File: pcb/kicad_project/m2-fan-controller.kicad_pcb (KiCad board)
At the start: 2 copper layers, 22 x 30 mm, 25 parts, among them J1 Bus_M.2_Socket_E, J2 JST PH_B4B-PH-K, J3 JST PH_B4B-PH-K, J4 JST PH_S2B-PH-K, J5 Conn_02x02_Odd_Even, U1 STM32F042F6P6, U2 TPS22810DBV, U3 TPS22810DBV

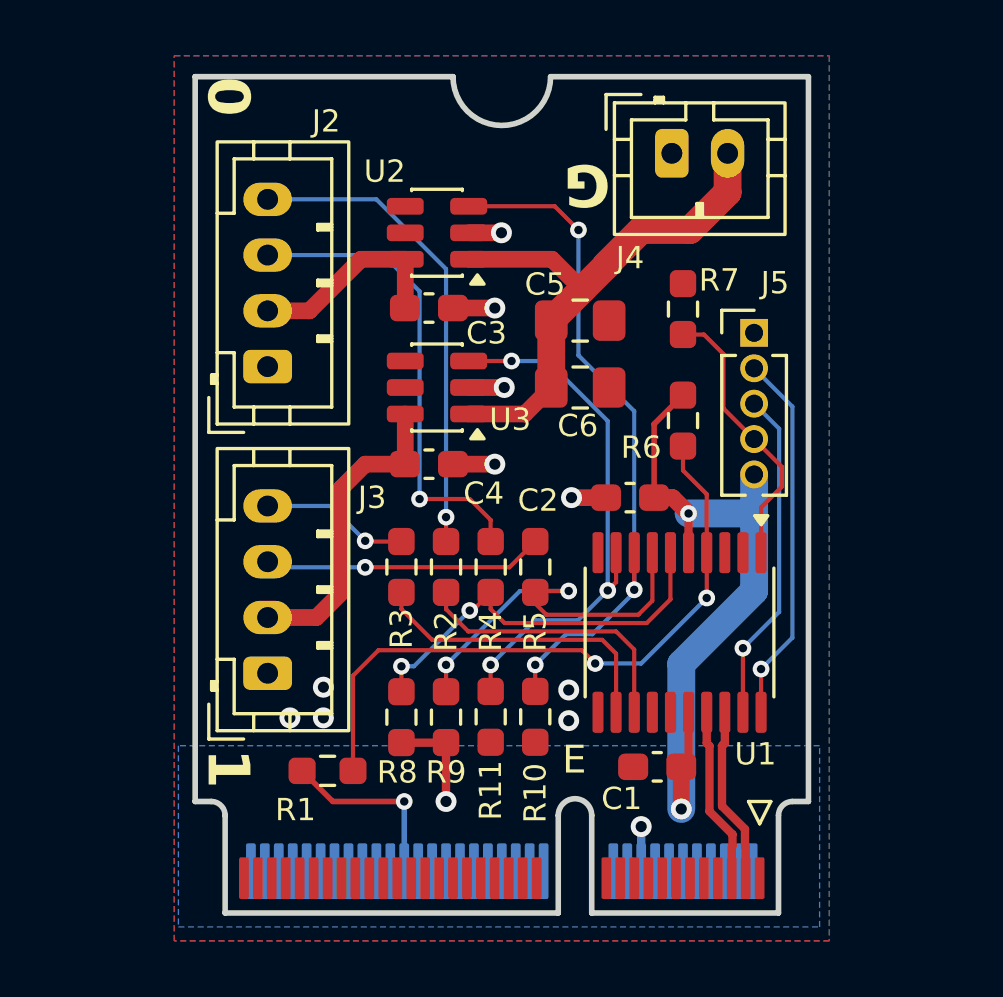
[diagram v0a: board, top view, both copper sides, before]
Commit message: Add 4-ouptut capability + low-frequency PWM control
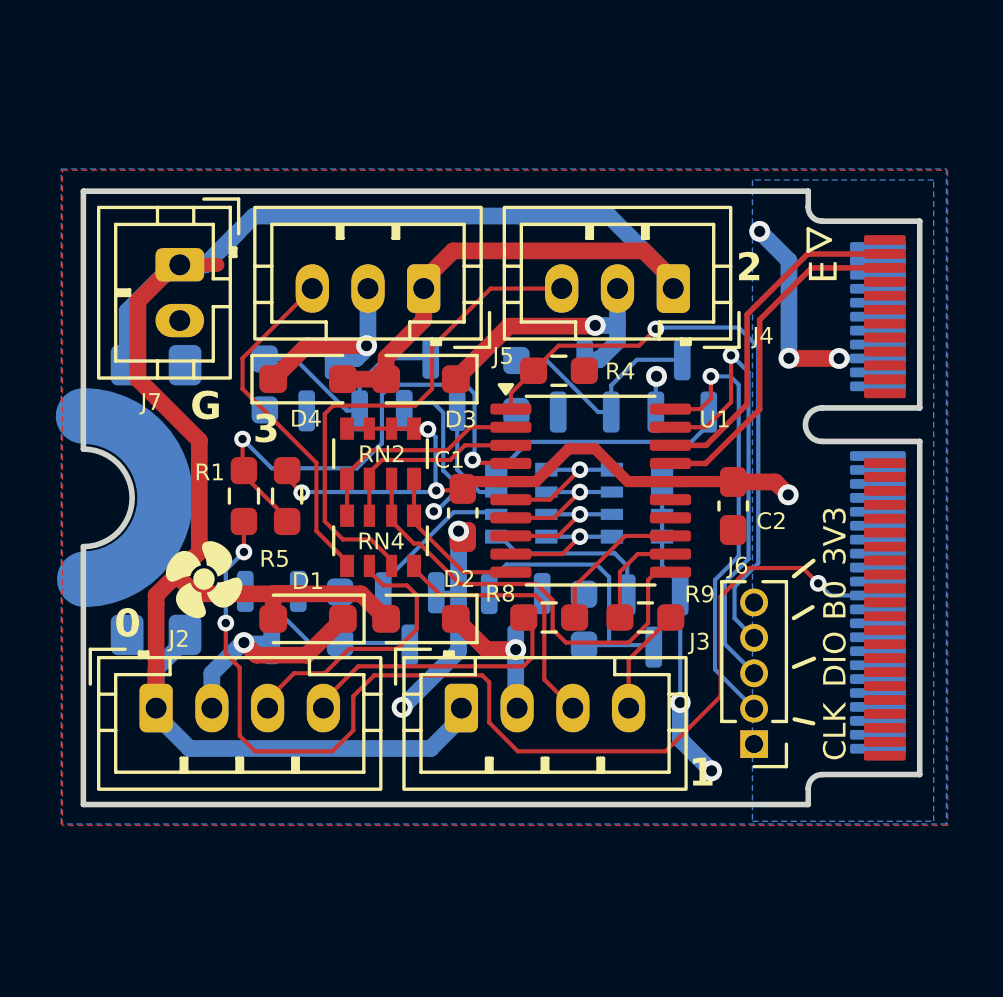
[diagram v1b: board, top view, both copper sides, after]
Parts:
- removed C5, C6: 1uF, Capacitor_SMD:C_0805_2012Metric_Pad1.18x1.45mm_HandSolder
- removed R10, R11: 10kOhm, Resistor_SMD:R_0603_1608Metric_Pad0.98x0.95mm_HandSolder
- removed U2, U3: TPS22810DBV, Package_TO_SOT_SMD:SOT-23-6
- added D1: GDB5819WS, Diode_SMD:D_SOD-323_HandSoldering, F.Cu at (132.1, 99.5)
- added D2: GDB5819WS, Diode_SMD:D_SOD-323_HandSoldering, F.Cu at (136.1, 99.5)
- added D3: GDB5819WS, Diode_SMD:D_SOD-323_HandSoldering, F.Cu at (136.1, 90.8)
- added D4: GDB5819WS, Diode_SMD:D_SOD-323_HandSoldering, F.Cu at (132.1, 90.8)
- added J4: JST PH_B3B-PH-K, Connector_JST:JST_PH_B3B-PH-K_1x03_P2.00mm_Vertical, F.Cu at (145.2, 87.6)
- added J5: JST PH_B3B-PH-K, Connector_JST:JST_PH_B3B-PH-K_1x03_P2.00mm_Vertical, F.Cu at (136.2, 87.6)
- added NT1: NetTie_2, NetTie:NetTie-2_SMD_Pad0.5mm, F.Cu at (128.3, 86.8)
- added Q1: BSS138, Package_TO_SOT_SMD:SOT-23, B.Cu at (135.7, 99.5)
- added Q2: AO3401A, Package_TO_SOT_SMD:SOT-23, B.Cu at (130.7, 99.4)
- added Q3: BSS138, Package_TO_SOT_SMD:SOT-23, B.Cu at (144.4, 99.5)
- added Q4: AO3401A, Package_TO_SOT_SMD:SOT-23, B.Cu at (139.5, 99.5)
- added Q5: BSS138, Package_TO_SOT_SMD:SOT-23, B.Cu at (145.5, 91.1)
- added Q6: AO3401A, Package_TO_SOT_SMD:SOT-23, B.Cu at (142.0, 91.1)
- added Q7: BSS138, Package_TO_SOT_SMD:SOT-23, B.Cu at (136.4, 91.0)
- added Q8: AO3401A, Package_TO_SOT_SMD:SOT-23, B.Cu at (132.9, 91.0)
- added RN1: 1kOhm, Resistor_SMD:R_Array_Convex_4x0603, B.Cu at (139.7, 95.3)
- added RN2: 10kOhm, Resistor_SMD:R_Array_Convex_4x0603, F.Cu at (134.7, 93.5)
- added RN3: 10kOhm, Resistor_SMD:R_Array_Convex_4x0603, B.Cu at (143.8, 95.3)
- added RN4: 100Ohm, Resistor_SMD:R_Array_Convex_4x0603, F.Cu at (134.7, 96.7)
- C3, C4: value 0.1uF -> 1uF; footprint Capacitor_SMD:C_0603_1608Metric_Pad1.08x0.95mm_HandSolder -> Capacitor_SMD:C_0805_2012Metric_Pad1.18x1.45mm_HandSolder; moved to B.Cu
- R2, R3: value 100Ohm -> 4.7kOhm; moved to B.Cu
- R4, R5: value 100Ohm -> 10kOhm
- R6, R7: value 10kOhm -> 4.7kOhm; moved to B.Cu
- R8: value 10kOhm -> 1kOhm
- R9: value 10kOhm -> 100Ohm
- moved J7 18.1 mm to (127.5, 86.8), turned to -90 degrees
- moved J1 15.5 mm to (150.0, 95.1), turned to 90 degrees
- moved R7 15.2 mm to (130.5, 91.0), turned to -90 degrees
- moved J6 14.8 mm to (148.1, 103.9), turned to 180 degrees
- moved J2 12.9 mm to (126.6, 102.7), turned to 0 degrees
- moved C4 11.5 mm to (126.6, 100.0)
- moved C1 11.5 mm to (137.6, 95.7), turned to -90 degrees
- moved R1 10.3 mm to (129.8, 95.0), turned to -90 degrees
- moved C3 10.00 mm to (126.6, 90.3), turned to 180 degrees
- moved R5 9.26 mm to (131.3, 95.0), turned to -90 degrees
- moved R9 7.99 mm to (144.2, 99.4), turned to 0 degrees
- moved R4 7.45 mm to (141.1, 90.5), turned to 0 degrees
- moved J3 7.06 mm to (137.6, 102.7), turned to 0 degrees
- moved R3 6.82 mm to (141.9, 99.5)
- moved R8 6.39 mm to (140.7, 99.4), turned to 180 degrees
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- renumbered J5 to J6, J4 to J7
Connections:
- net SWCLK renamed /SWCLK
- net SWDIO renamed /SWDIO
- net USB_D+ renamed /USB_D+
- net USB_D- renamed /USB_D-
- C1 pad 1: +3.3V -> 3V3
- C2 pad 1: +3.3V -> 3V3
- C3 pad 1: Net-(J2-Pin_2) -> 12V
- C3 pad 2: GND -> FGND
- C4 pad 1: Net-(J3-Pin_2) -> 12V
- C4 pad 2: GND -> FGND
- J1 pad 2: +3.3V -> 3V3
- J1 pad 4: +3.3V -> 3V3
- J1 pad 72: +3.3V -> 3V3
- J1 pad 74: +3.3V -> 3V3
- J2 pad 1: GND -> FGND
- J2 pad 2: Net-(J2-Pin_2) -> /POWER_0
- J3 pad 1: GND -> FGND
- J3 pad 2: Net-(J3-Pin_2) -> /POWER_1
- J6 pad 4: BOOT0 -> /BOOT0
- J6 pad 5: +3.3V -> 3V3
- J7 pad 1: GND -> FGND
- J7 pad 2: +12V -> 12V
- R1 pad 1: RST -> /RST
- R2 pad 1: PWM_0 -> Net-(Q1-D)
- R2 pad 2: Net-(J2-Pin_4) -> 12V
- R3 pad 1: PWM_1 -> Net-(Q3-D)
- R3 pad 2: Net-(J3-Pin_4) -> 12V
- R4 pad 1: TACH_0 -> /BOOT0
- R4 pad 2: Net-(J2-Pin_3) -> GND
- R5 pad 1: TACH_1 -> 3V3
- R5 pad 2: Net-(J3-Pin_3) -> /RST
- R6 pad 1: +3.3V -> Net-(Q5-D)
- R6 pad 2: RST -> 12V
- R7 pad 1: BOOT0 -> Net-(Q7-D)
- R7 pad 2: GND -> 12V
- R8 pad 1: +3.3V -> /PWM_0
- R8 pad 2: TACH_0 -> Net-(J2-Pin_4)
- R9 pad 1: +3.3V -> /PWM_1
- R9 pad 2: TACH_1 -> Net-(J3-Pin_4)
- U1 pad 1: BOOT0 -> /BOOT0
- U1 pad 10: unconnected-(U1-PA4-Pad10) -> /TACH_1
- U1 pad 11: unconnected-(U1-PA5-Pad11) -> /TACH_2
- U1 pad 12: PWM_1 -> /PWM_1
- U1 pad 13: PWM_0 -> /PWM_0
- U1 pad 16: +3.3V -> 3V3
- U1 pad 2: unconnected-(U1-PF0-Pad2) -> /TACH_3
- U1 pad 3: unconnected-(U1-PF1-Pad3) -> /TACH_0
- U1 pad 4: RST -> /RST
- U1 pad 5: +3.3V -> 3V3
- U1 pad 6: TACH_0 -> /EN_2
- U1 pad 7: TACH_1 -> /EN_3
- U1 pad 8: EN_0 -> /EN_0
- U1 pad 9: EN_1 -> /EN_1
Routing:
- net FGND: track 0.00 -> 84.8 mm
- net Net-(J1-~{PERST0}): track 6.62 -> 40.3 mm, vias 1 -> 3
- net +3.3V: track 29.3 -> 0.00 mm, vias 3 -> 0
- net GND: track 7.94 -> 34.9 mm, vias 11 -> 9
- net 3V3: track 0.00 -> 25.2 mm, vias 0 -> 4
- net EN_0: track 24.8 -> 0.00 mm, vias 3 -> 0
- net RST: track 23.0 -> 0.00 mm, vias 2 -> 0
- net /BOOT0: track 0.00 -> 21.8 mm, vias 0 -> 1
- net +12V: track 19.9 -> 0.00 mm
- net EN_1: track 19.4 -> 0.00 mm, vias 3 -> 0
- net /RST: track 0.00 -> 18.6 mm, vias 0 -> 2
- net Net-(J4-Pin_3): track 0.00 -> 18.3 mm
- net /TACH_2: track 0.00 -> 15.8 mm
- net TACH_0: track 14.5 -> 0.00 mm, vias 2 -> 0
- net TACH_1: track 14.4 -> 0.00 mm, vias 2 -> 0
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- added copper zone on B.Cu, net 12V
- added copper zone on B.Cu, net 3V3
- removed copper zone on B.Cu, net +3.3V
- removed copper zone on B.Cu, net GND
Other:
- board size 22 x 30 mm -> 30 x 22 mm
- board text added: "(c) 2026 Sergio Carmine"
- board text added: "2"
- board text added: "3"
- board text added: "3V3"
- board text added: "B0"
- board text added: "CLK"
- board text added: "DIO"
- board text removed: "(c) 2026 - Sergio Carmine"
- board text removed: "3.3V"
- board text removed: "BOOT0"
- board text removed: "SWCLK"
- board text removed: "SWDIO"

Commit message: 4 layer layout
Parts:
- removed NT1: NetTie_2, NetTie:NetTie-2_SMD_Pad0.5mm
- moved C3 6.83 mm to (132.2, 94.3)
- moved C4 6.74 mm to (132.2, 96.3), turned to 180 degrees
- moved RN2 0.85 mm to (133.8, 93.5)
- moved RN4 0.85 mm to (133.8, 96.7)
- moved R1 0.65 mm to (129.1, 95.0)
- moved R5 0.65 mm to (130.7, 95.0), turned to 90 degrees
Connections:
- C3 pad 2: FGND -> GND
- C4 pad 2: FGND -> GND
- D1 pad 2: FGND -> GND
- D2 pad 2: FGND -> GND
- D3 pad 2: FGND -> GND
- D4 pad 2: FGND -> GND
- J2 pad 1: FGND -> GND
- J3 pad 1: FGND -> GND
- J4 pad 1: FGND -> GND
- J5 pad 1: FGND -> GND
- J6 pad 2: /SWCLK -> /SWDIO
- J6 pad 3: /SWDIO -> /SWCLK
- J7 pad 1: FGND -> GND
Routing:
- net FGND: track 84.8 -> 0.00 mm
- net 3V3: track 25.2 -> 45.7 mm
- net GND: track 34.9 -> 18.6 mm, vias 9 -> 17
- net /RST: track 18.6 -> 12.8 mm
- net Net-(J2-Pin_3): track 10.2 -> 7.48 mm
- net /TACH_1: track 5.74 -> 7.22 mm
- net /TACH_2: track 15.8 -> 17.2 mm
- net Net-(Q1-G): track 5.49 -> 6.65 mm
- net /TACH_0: track 7.03 -> 8.15 mm
- net /TACH_3: track 8.06 -> 9.16 mm
- net Net-(J3-Pin_3): track 9.45 -> 10.4 mm
- net Net-(J1-~{PERST0}): track 40.3 -> 39.6 mm, vias 3 -> 1
- net /BOOT0: track 21.8 -> 21.2 mm
- net Net-(J4-Pin_3): track 18.3 -> 18.8 mm
- added copper zone on B.Cu, net GND
- added copper zone on In1.Cu, net GND
- added copper zone on In2.Cu, net GND
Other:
- copper layers 2 -> 4

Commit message: Final production layout
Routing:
- net /POWER_3: track 7.37 -> 9.03 mm, vias 1 -> 0
- net /POWER_2: track 9.94 -> 10.6 mm, vias 1 -> 0
- net Net-(J2-Pin_4): track 9.81 -> 9.27 mm
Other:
- board text removed: "G"

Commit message: Change P-channel mosfets to AO3407A
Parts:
- Q2, Q4, Q6, Q8: value AO3401A -> AO3407A
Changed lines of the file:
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@@
 		(sheetname "/")
 		(sheetfile "m2-fan-controller.kicad_sch")
+		(units
+			(unit
+				(name "A")
+				(pins "52" "53" "55" "35" "37" "41" "43" "59" "61" "65" "67" "3" "5"
+					"66" "68" "70" "9" "11" "13" "15" "17" "19" "21" "23" "47" "49" "71"
+					"73" "72" "74" "4" "2" "63" "69" "57" "1" "51" "75" "7" "45" "33" "18"
+					"39" "64" "38" "40" "42" "58" "60" "62" "56" "54" "8" "10" "12" "14"
+					"20" "22" "32" "34" "36" "6" "16" "50" "48" "46" "44"
+				)
+			)
+		)
 		(clearance 0.1)
 		(duplicate_pad_numbers_are_jumpers no)
@@
 			)
 		)
-		(property "Value" "AO3401A"
+		(property "Value" "AO3407A"
 			(at 0 -2.4 90)
 			(layer "B.Fab")
@@
 			)
 		)
-		(property "Value" "AO3401A"
+		(property "Value" "AO3407A"
 			(at 0 -2.4 90)
 			(layer "B.Fab")
@@
 			)
 		)
-		(property "Value" "AO3401A"
+		(property "Value" "AO3407A"
 			(at 0 -2.4 90)
 			(layer "B.Fab")
@@
 			)
 		)
-		(property "Value" "AO3401A"
+		(property "Value" "AO3407A"
 			(at 0 -2.4 90)
 			(layer "B.Fab")
@@
 		(sheetname "/")
 		(sheetfile "m2-fan-controller.kicad_sch")
+		(units
+			(unit
+				(name "A")
+				(pins "1" "3" "2")
+			)
+		)
 		(attr smd)
 		(duplicate_pad_numbers_are_jumpers no)
